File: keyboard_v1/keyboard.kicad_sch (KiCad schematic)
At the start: 52 parts, among them J1 BOOT0, J2 SWD, J3 UART, J4 rs485, SW31 SW_Push, U1 STM32F030C8Tx, U2 74HC595, U3 SP3485EN, Y1 X322516MLB4SI

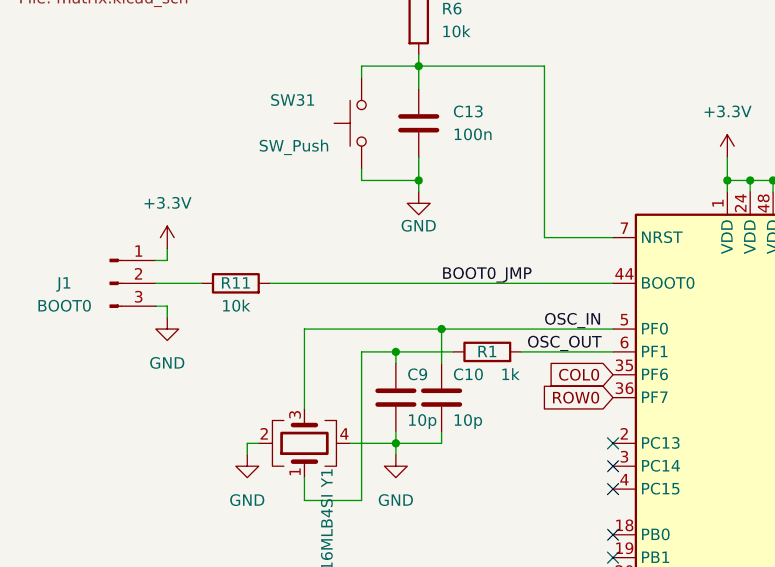
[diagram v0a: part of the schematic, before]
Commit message: remove boot selector on keyboard
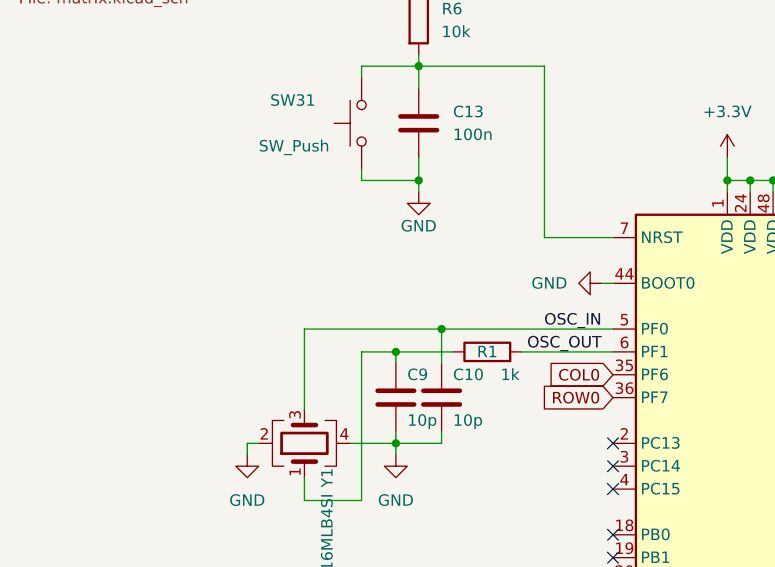
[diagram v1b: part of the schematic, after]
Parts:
- removed J1: BOOT0, Connector_PinHeader_1.27mm:PinHeader_1x03_P1.27mm_Vertical, symbol Connector:Conn_01x03_Pin
- removed R11: 10k, Resistor_SMD:R_0402_1005Metric, symbol Device:R
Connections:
- net BOOT0_JMP is gone; now on net GND: U1.44 (BOOT0)
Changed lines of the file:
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@@
-    (stroke (width 0) (type default))
-  )
-  (wire (pts (xy 36.83 71.12) (xy 36.83 72.39))
     (stroke (width 0) (type default))
   )
@@
     (stroke (width 0) (type default))
   )
-  (wire (pts (xy 35.56 77.47) (xy 36.83 77.47))
-    (stroke (width 0) (type default))
-  )
   (wire (pts (xy 273.05 45.72) (xy 273.05 48.26))
     (stroke (width 0) (type default))
@@
     (stroke (width 0) (type default))
   )
+  (wire (pts (xy 85.09 74.93) (xy 86.36 74.93))
+    (stroke (width 0) (type default))
+  )
   (wire (pts (xy 261.62 83.82) (xy 261.62 85.09))
     (stroke (width 0) (type default))
@@
     (stroke (width 0) (type default))
   )
-  (wire (pts (xy 36.83 72.39) (xy 35.56 72.39))
-    (stroke (width 0) (type default))
-  )
   (wire (pts (xy 58.42 62.23) (xy 58.42 63.5))
     (stroke (width 0) (type default))
@@
     (stroke (width 0) (type default))
   )
-  (wire (pts (xy 48.26 74.93) (xy 86.36 74.93))
-    (stroke (width 0) (type default))
-  )
   (wire (pts (xy 224.79 83.82) (xy 224.79 85.09))
     (stroke (width 0) (type default))
@@
     (stroke (width 0) (type default))
   )
-  (wire (pts (xy 36.83 77.47) (xy 36.83 78.74))
-    (stroke (width 0) (type default))
-  )
   (wire (pts (xy 119.38 50.8) (xy 128.27 50.8))
     (stroke (width 0) (type default))
@@
   )
   (wire (pts (xy 67.31 80.01) (xy 67.31 83.82))
-    (stroke (width 0) (type default))
-  )
-  (wire (pts (xy 35.56 74.93) (xy 40.64 74.93))
     (stroke (width 0) (type default))
   )
@@
   (label "OSC_OUT" (at 85.09 82.55 180) (fields_autoplaced)
     (effects (font (size 1.27 1.27)) (justify right bottom))
-  )
-  (label "BOOT0_JMP" (at 67.31 74.93 0) (fields_autoplaced)
-    (effects (font (size 1.27 1.27)) (justify left bottom))
   )
   (label "OSC_IN" (at 85.09 80.01 180) (fields_autoplaced)
@@
     )
   )
+  (symbol (lib_id "power:GND") (at 85.09 74.93 270) (unit 1)
+    (in_bom yes) (on_board yes) (dnp no) (fields_autoplaced)
+    (property "Reference" "#PWR07" (at 78.74 74.93 0)
+      (effects (font (size 1.27 1.27)) hide)
+    )
+    (property "Value" "GND" (at 81.28 74.93 90)
+      (effects (font (size 1.27 1.27)) (justify right))
+    )
+    (property "Footprint" "" (at 85.09 74.93 0)
+      (effects (font (size 1.27 1.27)) hide)
+    )
+    (property "Datasheet" "" (at 85.09 74.93 0)
+      (effects (font (size 1.27 1.27)) hide)
+    )
+    (pin "1")
+    (instances
+      (project "keyboard"
+        (path "/8e2587f0-571c-4ce0-a7a5-c33de315eb65"
+          (reference "#PWR07") (unit 1)
+        )
+      )
+    )
+  )
   (symbol (lib_id "power:GND") (at 45.72 93.98 0) (unit 1)
     (in_bom yes) (on_board yes) (dnp no) (fields_autoplaced)
@@
     )
   )
-  (symbol (lib_id "Connector:Conn_01x03_Pin") (at 30.48 74.93 0) (unit 1)
-    (in_bom yes) (on_board yes) (dnp no)
-    (property "Reference" "J1" (at 25.4 74.93 0)
-      (effects (font (size 1.27 1.27)))
-    )
-    (property "Value" "BOOT0" (at 25.4 77.47 0)
-      (effects (font (size 1.27 1.27)))
-    )
-    (property "Footprint" "Connector_PinHeader_1.27mm:PinHeader_1x03_P1.27mm_Vertical" (at 30.48 74.93 0)
-      (effects (font (size 1.27 1.27)) hide)
-    )
-    (property "Datasheet" "~" (at 30.48 74.93 0)
-      (effects (font (size 1.27 1.27)) hide)
-    )
-    (pin "1")
-    (pin "2")
-    (pin "3")
-    (instances
-      (project "keyboard"
-        (path "/8e2587f0-571c-4ce0-a7a5-c33de315eb65"
-          (reference "J1") (unit 1)
-        )
-      )
-    )
-  )
   (symbol (lib_id "Device:C") (at 143.51 55.88 0) (unit 1)
     (in_bom yes) (on_board yes) (dnp no)
@@
     )
   )
-  (symbol (lib_id "power:+3.3V") (at 36.83 71.12 0) (unit 1)
-    (in_bom yes) (on_board yes) (dnp no) (fields_autoplaced)
-    (property "Reference" "#PWR07" (at 36.83 74.93 0)
-      (effects (font (size 1.27 1.27)) hide)
-    )
-    (property "Value" "+3.3V" (at 36.83 66.04 0)
-      (effects (font (size 1.27 1.27)))
-    )
-    (property "Footprint" "" (at 36.83 71.12 0)
-      (effects (font (size 1.27 1.27)) hide)
-    )
-    (property "Datasheet" "" (at 36.83 71.12 0)
-      (effects (font (size 1.27 1.27)) hide)
-    )
-    (pin "1")
-    (instances
-      (project "keyboard"
-        (path "/8e2587f0-571c-4ce0-a7a5-c33de315eb65"
-          (reference "#PWR07") (unit 1)
-        )
-      )
-    )
-  )
   (symbol (lib_id "Device:C") (at 149.86 55.88 0) (unit 1)
     (in_bom yes) (on_board yes) (dnp no)
@@
         )
       )
-    )
-  )
-  (symbol (lib_id "power:GND") (at 36.83 78.74 0) (unit 1)
-    (in_bom yes) (on_board yes) (dnp no) (fields_autoplaced)
-    (property "Reference" "#PWR08" (at 36.83 85.09 0)
-      (effects (font (size 1.27 1.27)) hide)
-    )
-    (property "Value" "GND" (at 36.83 83.82 0)
-      (effects (font (size 1.27 1.27)))
-    )
-    (property "Footprint" "" (at 36.83 78.74 0)
-      (effects (font (size 1.27 1.27)) hide)
-    )
-    (property "Datasheet" "" (at 36.83 78.74 0)
-      (effects (font (size 1.27 1.27)) hide)
-    )
-    (pin "1")
-    (instances
-      (project "keyboard"
-        (path "/8e2587f0-571c-4ce0-a7a5-c33de315eb65"
-          (reference "#PWR08") (unit 1)
-        )
-      )
-    )
-  )
-  (symbol (lib_id "Device:R") (at 44.45 74.93 90) (unit 1)
-    (in_bom yes) (on_board yes) (dnp no)
-    (property "Reference" "R11" (at 44.45 74.93 90)
-      (effects (font (size 1.27 1.27)))
-    )
-    (property "Value" "10k" (at 44.45 77.47 90)
-      (effects (font (size 1.27 1.27)))
-    )
-    (property "Footprint" "Resistor_SMD:R_0402_1005Metric" (at 44.45 76.708 90)
-      (effects (font (size 1.27 1.27)) hide)
-    )
-    (property "Datasheet" "~" (at 44.45 74.93 0)
-      (effects (font (size 1.27 1.27)) hide)
-    )
-    (property "LCSC" "C25744" (at 44.45 74.93 0)
-      (effects (font (size 1.27 1.27)) hide)
-    )
-    (property "jlc_url" "https://jlcpcb.com/partdetail/26487-0402WGF1002TCE/C25744" (at 44.45 74.93 0)
-      (effects (font (size 1.27 1.27)) hide)
-    )
-    (pin "1")
-    (pin "2")
-    (instances
-      (project "keyboard"
-        (path "/8e2587f0-571c-4ce0-a7a5-c33de315eb65"
-          (reference "R11") (unit 1)
-        )
-      )
